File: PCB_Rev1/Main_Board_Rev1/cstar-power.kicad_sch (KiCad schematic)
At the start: 52 parts, among them IC1 LT8648SEV#PBF, J14 USB4125-GF-A_REVA2, J4 Conn_01x02_Pin, J5 XT60PW-M, J6 Conn_01x02_Pin, J7 Conn_01x02_Pin, J8 Conn_01x02_Pin, U1 AZ1117IH-3.3TRG1

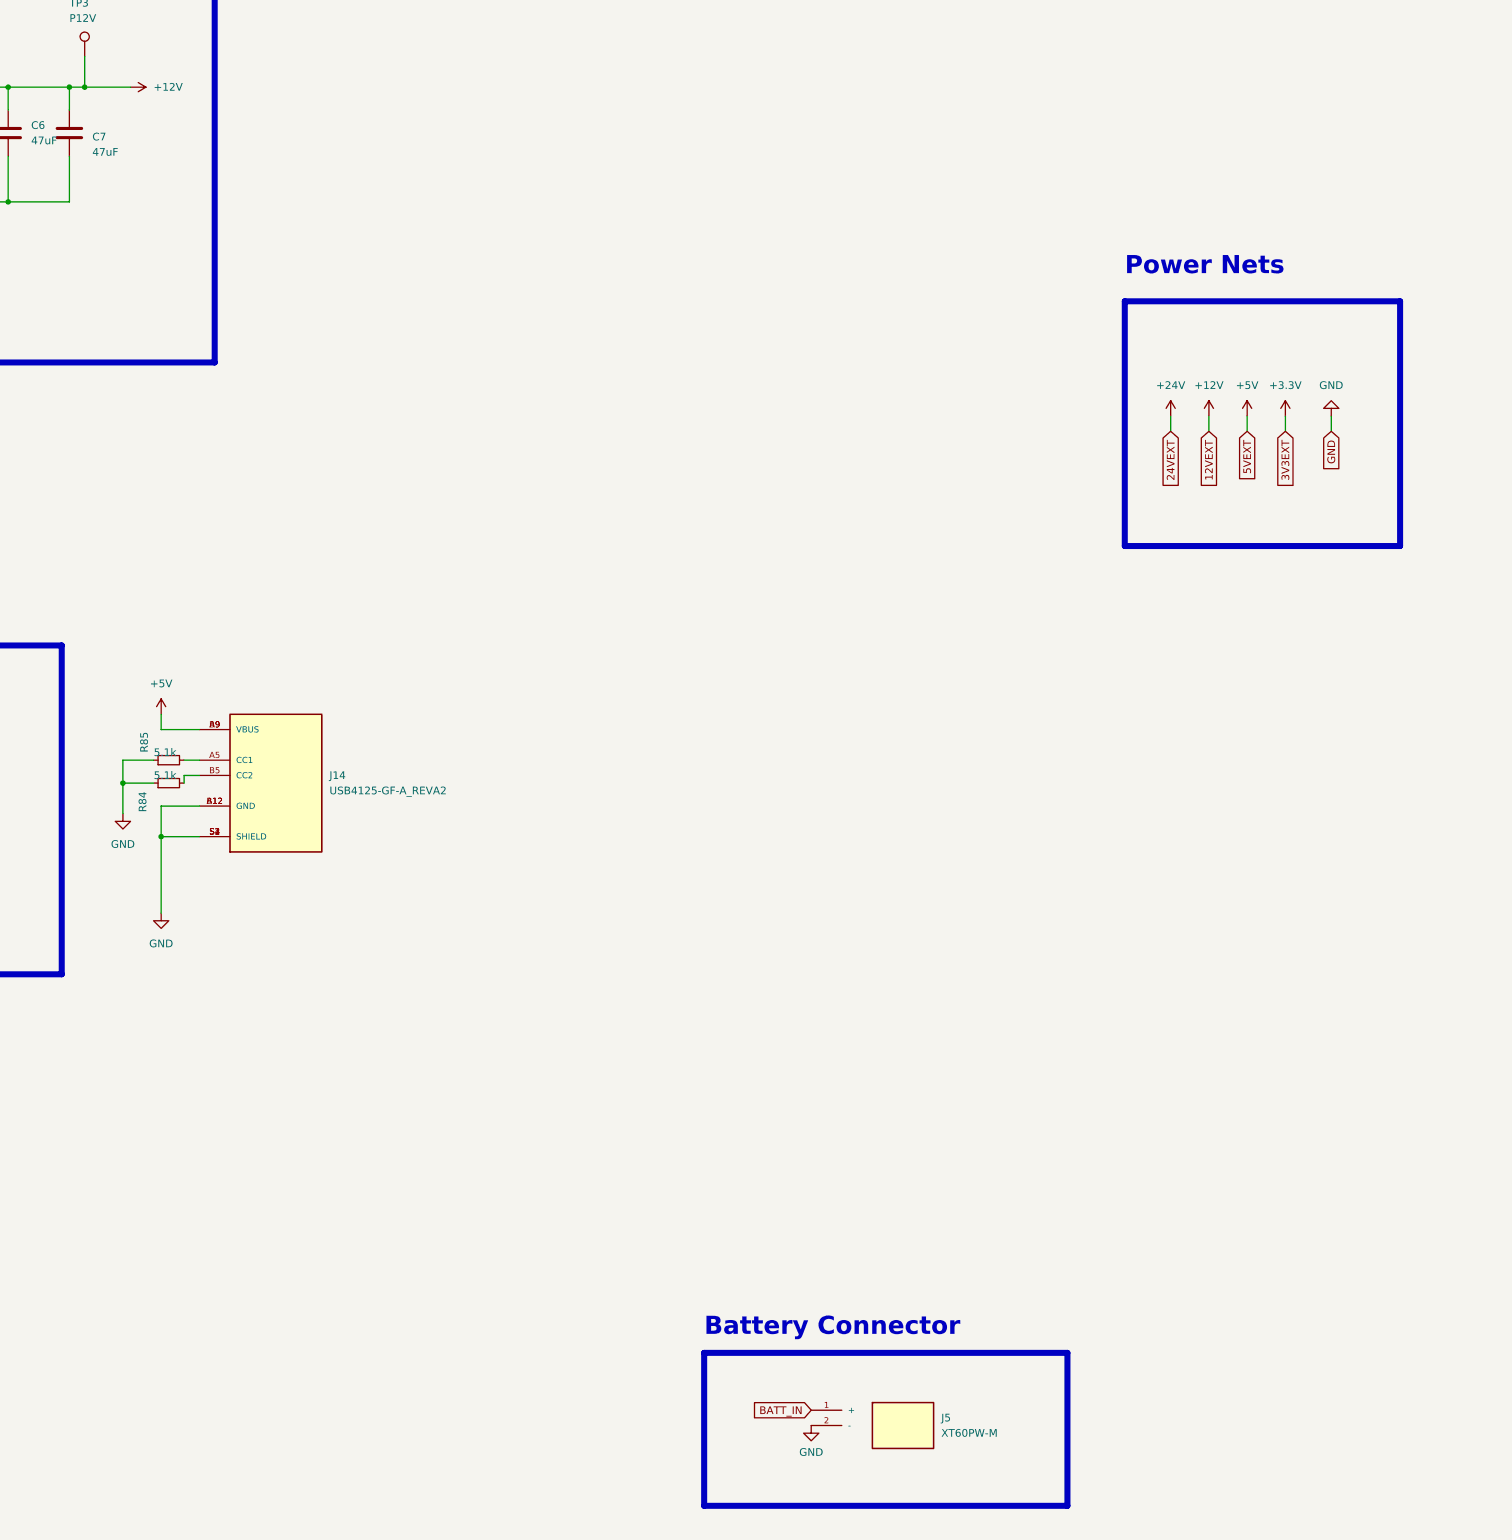
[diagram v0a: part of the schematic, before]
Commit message: ESD Protection for USB Connector
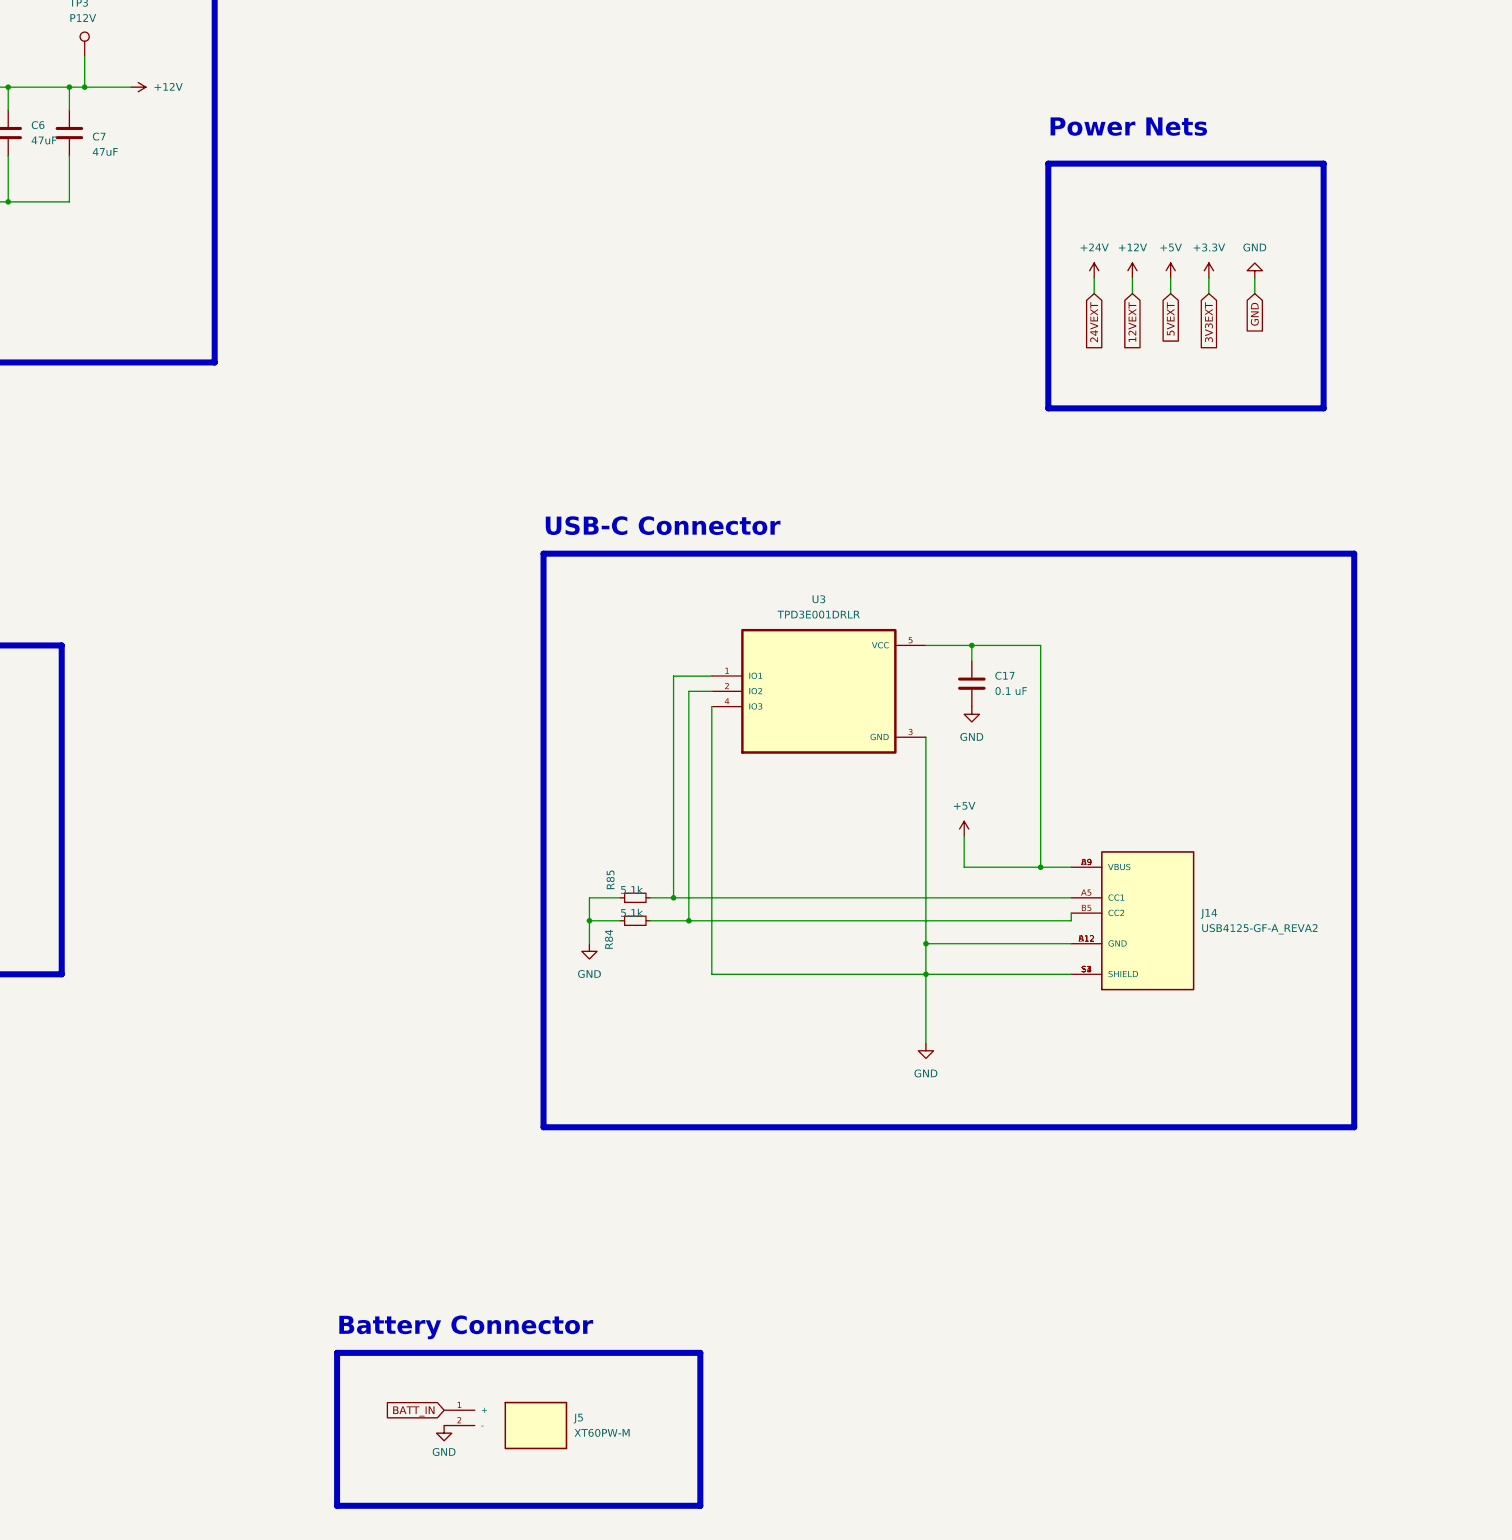
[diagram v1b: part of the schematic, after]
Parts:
- added C17: 0.1 uF, Capacitor_SMD:C_0805_2012Metric, symbol Device:C
- added U3: TPD3E001DRLR, Footprints:USBC_ESD_Protection, symbol USB-Diode:TPD3E001DRLR
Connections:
- net +5V: now also C17.1, U3.5 (VCC)
- net GND: now also C17.2, U3.3 (GND), U3.4 (IO3)
- net at J14.A5 (CC1), R85.2: now also U3.1 (IO1)
- net at J14.B5 (CC2), R84.2: now also U3.2 (IO2)
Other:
- note added: "USB-C Connector"
- moved on the sheet: J14, J5, R84, R85

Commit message: LCSC + CSV changes
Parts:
- C10, C4, C8: LCSC (none) -> C2190942
- C11, C17: LCSC (none) -> C49678
- C12: LCSC (none) -> C107118
- C13, C14, C9: LCSC (none) -> C602037
- C2: LCSC (none) -> C116352
- C3: LCSC (none) -> C2167084
- C5: LCSC (none) -> C527074
- C6, C7: LCSC (none) -> C2167787
- D1: LCSC (none) -> C151280
- F1: LCSC (none) -> C3158319
- F2, F3: LCSC (none) -> C3159342
- IC1: LCSC (none) -> C2840907
- J14: LCSC (none) -> C5246813
- J4, J6, J7, J8: LCSC (none) -> C5828287
- J5: LCSC (none) -> C98732
- L1: LCSC (none) -> C540967
- L2: LCSC (none) -> C844992
- LED1, LED2, LED3, LED4: footprint Footprints:LED_0VS75000_WRE -> LED_SMD:LED_0805_2012Metric
- PS1: LCSC (none) -> C3194571
- R10: LCSC (none) -> C483083
- R11: LCSC (none) -> C273808
- R12: LCSC (none) -> C273954
- R13: LCSC (none) -> C126352
- R3: LCSC (none) -> C273997
- R4: LCSC (none) -> C273910
- R5: LCSC (none) -> C273970
- R7: LCSC (none) -> C96346
- R8: LCSC (none) -> C274009
- R84, R85: LCSC (none) -> C105874
- R9: LCSC (none) -> C137416
- U1: LCSC (none) -> C108495
- U3: LCSC (none) -> C470828
